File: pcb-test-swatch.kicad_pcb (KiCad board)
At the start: 2 copper layers, 18 x 18 mm, 4 parts

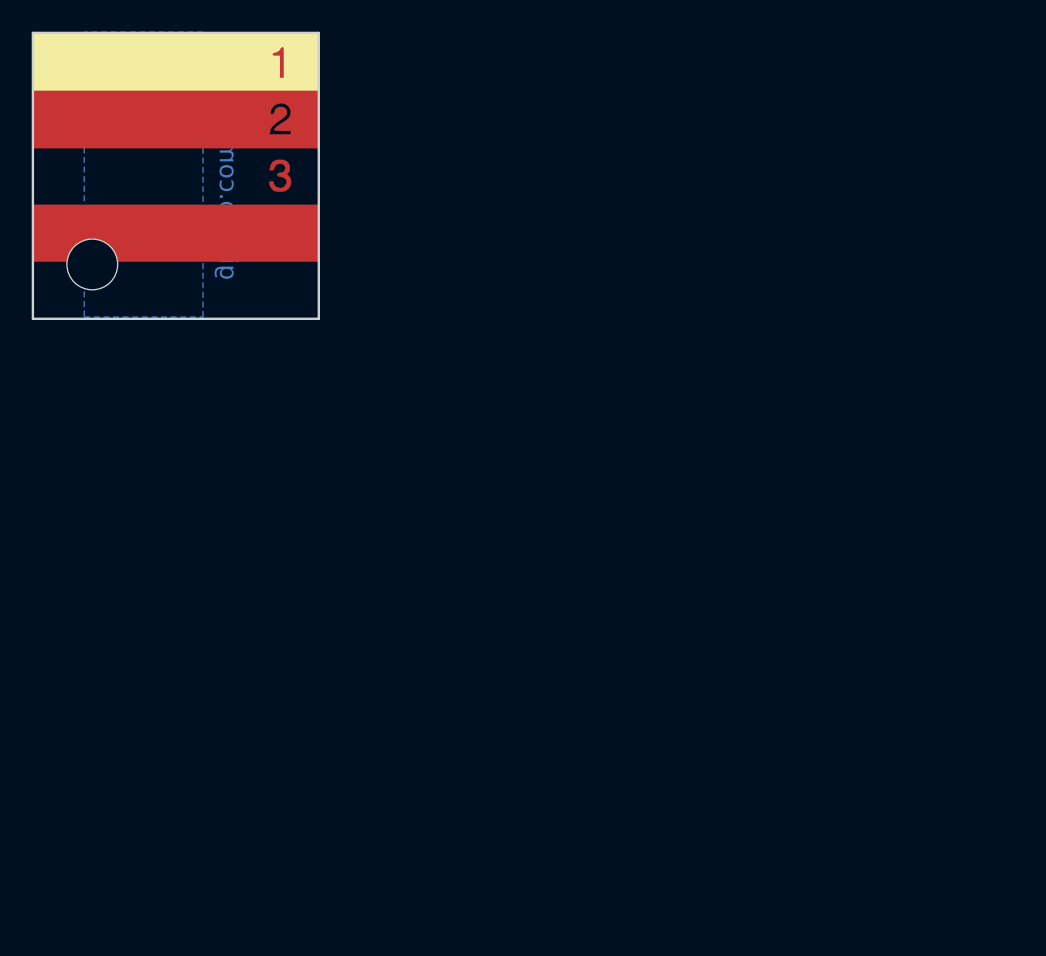
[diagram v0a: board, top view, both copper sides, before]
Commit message: Put mask on correct side of back layer
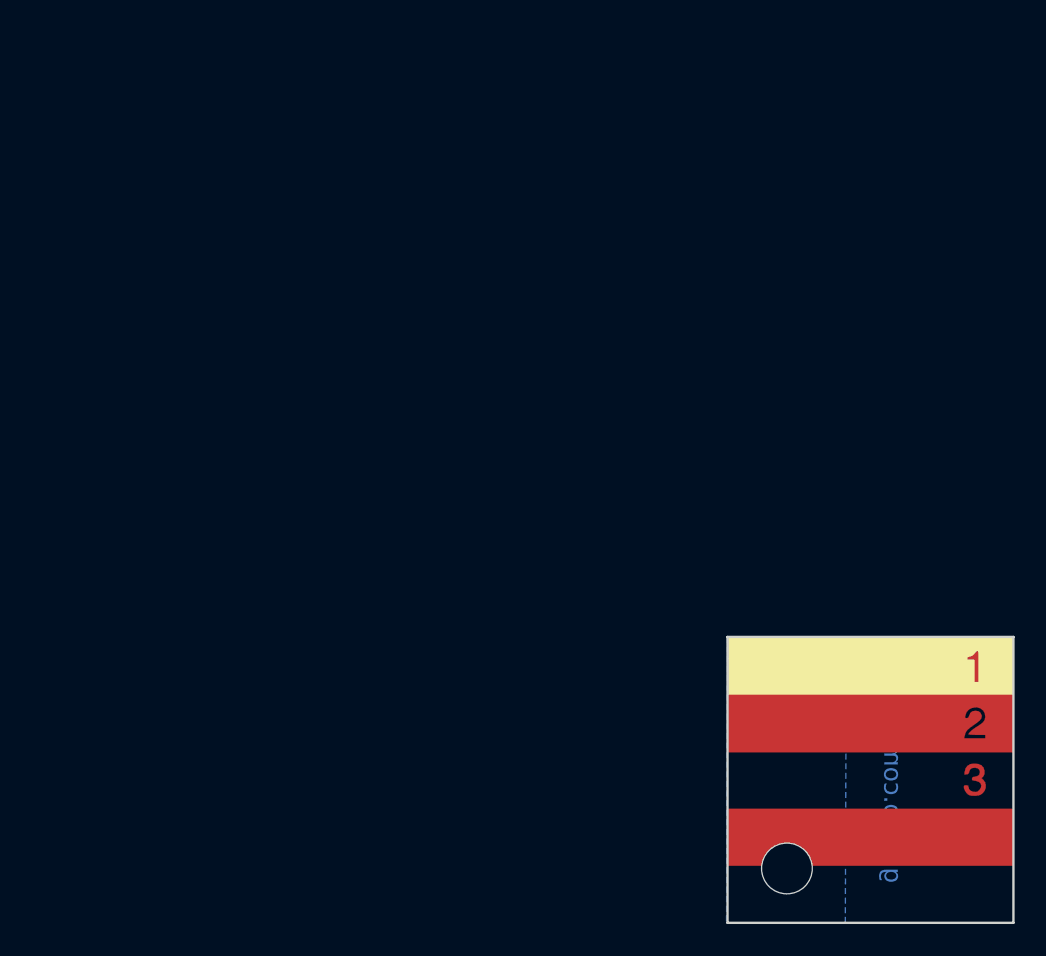
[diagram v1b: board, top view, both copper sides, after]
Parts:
- moved G*** 58.1 mm to (43.8, 38.1) (x3)
- moved REF** 58.1 mm to (38.5, 43.7)
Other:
- board text added: "PCB LAYER TEST"
- board text added: "Remember: The solder mask layers in kicad act as a solder mask mask, so wherever you draw on the soldermask layer in kicad, no mask will appear on the PCB!"
- board text added: "copper [number is mask on copper]"
- board text added: "mask [number: copper under mask]"
- board text added: "mask on copper [number:hole in copper]"
- board text added: "nothing (bare pcb), number is mask"
- board text added: "silk on mask on copper [number: hole in silk]"
- board text removed: "LAYER TEST"
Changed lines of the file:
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@@
   (general
     (thickness 1.6)
-    (drawings 6)
+    (drawings 12)
     (tracks 0)
     (zones 0)
@@
     (0 F.Cu signal)
     (31 B.Cu signal)
-    (32 B.Adhes user hide)
-    (33 F.Adhes user hide)
-    (34 B.Paste user hide)
-    (35 F.Paste user hide)
+    (32 B.Adhes user)
+    (33 F.Adhes user)
+    (34 B.Paste user)
+    (35 F.Paste user)
     (36 B.SilkS user)
     (37 F.SilkS user)
     (38 B.Mask user)
     (39 F.Mask user)
-    (40 Dwgs.User user hide)
-    (41 Cmts.User user hide)
-    (42 Eco1.User user hide)
-    (43 Eco2.User user hide)
+    (40 Dwgs.User user)
+    (41 Cmts.User user)
+    (42 Eco1.User user)
+    (43 Eco2.User user)
     (44 Edge.Cuts user)
-    (45 Margin user hide)
-    (46 B.CrtYd user hide)
-    (47 F.CrtYd user hide)
-    (48 B.Fab user hide)
-    (49 F.Fab user hide)
+    (45 Margin user)
+    (46 B.CrtYd user)
+    (47 F.CrtYd user)
+    (48 B.Fab user)
+    (49 F.Fab user)
   )
   (setup
     (last_trace_width 0.25)
     (trace_clearance 0.2)
-    (zone_clearance 0.508)
+    (zone_clearance 0)
     (zone_45_only no)
     (trace_min 0.2)
@@
   )
   (module MountingHole:MountingHole_3.2mm_M3 (layer F.Cu)
-    (at -5.2705 5.588)
+    (at 38.5445 43.688)
     (descr "Mounting Hole 3.2mm, no annular, M3")
     (tags "mounting hole 3.2mm no annular m3")
@@
   )
   (module LOGO (layer F.Cu)
-    (at 0 0)
+    (at 43.815 38.1)
     (fp_text reference G*** (at 0 0) (layer F.SilkS) hide
       (effects (font (size 1.524 1.524) (thickness 0.3)))
@@
   )
   (module LOGO (layer F.Cu)
-    (at 0 0)
+    (at 43.815 38.1)
     (fp_text reference G*** (at 0 0) (layer F.SilkS) hide
       (effects (font (size 1.524 1.524) (thickness 0.3)))
@@
   )
   (module LOGO (layer F.Cu)
-    (at 0 0)
+    (at 43.815 38.1)
     (fp_text reference G*** (at 0 0) (layer F.SilkS) hide
       (effects (font (size 1.524 1.524) (thickness 0.3)))
@@
       (xy 6.626142 2.960415)) (layer F.Mask) (width 0.01))
   )
-  (gr_text github.com/joem (at 3.302 -0.0635 270) (layer B.Cu)
+  (gr_text "Remember: The solder mask layers in kicad act as a solder mask mask, so wherever\nyou draw on the soldermask layer in kicad, no mask will appear on the PCB!" (at 59.563 57.531) (layer Dwgs.User)
+    (effects (font (size 1.2 1.2) (thickness 0.15) italic))
+  )
+  (gr_text "nothing (bare pcb), number is mask" (at 53.697095 45.085) (layer Dwgs.User)
+    (effects (font (size 1 1) (thickness 0.15)) (justify left))
+  )
+  (gr_text "copper [number is mask on copper]" (at 53.697095 41.4655) (layer Dwgs.User)
+    (effects (font (size 1 1) (thickness 0.15)) (justify left))
+  )
+  (gr_text "mask [number: copper under mask]" (at 53.697095 37.846) (layer Dwgs.User)
+    (effects (font (size 1 1) (thickness 0.15)) (justify left))
+  )
+  (gr_text "mask on copper [number:hole in copper]" (at 53.697095 34.2265) (layer Dwgs.User)
+    (effects (font (size 1 1) (thickness 0.15)) (justify left))
+  )
+  (gr_text "silk on mask on copper [number: hole in silk]" (at 53.697095 30.607) (layer Dwgs.User)
+    (effects (font (size 1 1) (thickness 0.15)) (justify left))
+  )
+  (gr_text github.com/joem (at 45.212 37.973 270) (layer B.Cu)
     (effects (font (size 1.143 1.143) (thickness 0.2032)) (justify mirror))
   )
-  (gr_text "LAYER TEST" (at -0.254 -0.508 270) (layer B.SilkS)
+  (gr_text "PCB LAYER TEST" (at 43.18 37.719 270) (layer B.SilkS)
     (effects (font (size 1 1) (thickness 0.15)) (justify mirror))
   )
-  (gr_line (start -9.017 9.017) (end -9.017 -9.017) (layer Edge.Cuts) (width 0.15))
-  (gr_line (start 9.017 9.017) (end -9.017 9.017) (layer Edge.Cuts) (width 0.15))
-  (gr_line (start 9.017 -9.017) (end 9.017 9.017) (layer Edge.Cuts) (width 0.15))
-  (gr_line (start -9.017 -9.017) (end 9.017 -9.017) (layer Edge.Cuts) (width 0.15))
+  (gr_line (start 34.798 47.117) (end 34.798 29.083) (layer Edge.Cuts) (width 0.15))
+  (gr_line (start 52.832 47.117) (end 34.798 47.117) (layer Edge.Cuts) (width 0.15))
+  (gr_line (start 52.832 29.083) (end 52.832 47.117) (layer Edge.Cuts) (width 0.15))
+  (gr_line (start 34.798 29.083) (end 52.832 29.083) (layer Edge.Cuts) (width 0.15))
   (zone (net 0) (net_name "") (layer B.SilkS) (hatch edge 0.508)
     (connect_pads (clearance 0.508))
@@
     (polygon
       (pts
-        (xy -2.032 -8.981161) (xy -10.414 -8.981161) (xy -10.414 8.989339) (xy -1.9685 8.989339)
+        (xy 41.783 29.118839) (xy 34.798 29.11475) (xy 34.798 47.08525) (xy 41.8465 47.089339)
       )
     )
   )
   (zone (net 0) (net_name "") (layer B.Cu) (hatch edge 0.508)
+    (connect_pads (clearance 0))
+    (min_thickness 0.254)
+    (fill yes (arc_segments 32) (thermal_gap 0) (thermal_bridge_width 0.255))
+    (polygon
+      (pts
+        (xy 42.291 29.083) (xy 34.798 29.083) (xy 34.7345 47.117) (xy 42.2275 47.117)
+      )
+    )
+  )
+  (zone (net 0) (net_name "") (layer B.Mask) (hatch edge 0.508)
     (connect_pads (clearance 0.508))
     (min_thickness 0.254)
@@
     (polygon
       (pts
-        (xy 1.7145 -9.063361) (xy -5.7785 -9.063361) (xy -5.7785 8.907139) (xy 1.7145 8.907139)
+        (xy 52.832 29.083) (xy 34.798 29.083) (xy 34.798 47.117) (xy 52.832 47.117)
       )
     )

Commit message: Update project to kicad 6+
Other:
- net class Default removed
